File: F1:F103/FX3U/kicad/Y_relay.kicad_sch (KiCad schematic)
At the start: 3 parts, among them K2 HF46F

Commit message: End schematics
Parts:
- renumbered D25 to D30, K2 to K6, R3 to R75
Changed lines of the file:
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@@
 		(on_board yes)
 		(dnp no)
-		(property "Reference" "R3"
+		(property "Reference" "R75"
 			(at 64.135 46.99 90)
 			(effects
@@
 		(dnp no)
 		(fields_autoplaced yes)
-		(property "Reference" "K2"
+		(property "Reference" "K6"
 			(at 99.187 48.3178 0)
 			(effects
@@
 				(path "/b583aae5-8eb0-4221-b485-3f768bd7f89b/1c43d7a4-ec7a-47bb-8132-9a3f4ab13e61"
 					(reference "K9")
+					(unit 1)
+				)
+				(path "/b583aae5-8eb0-4221-b485-3f768bd7f89b/448100fa-8d41-4af2-bc0f-6a1f6a77b73d"
+					(reference "K1")
 					(unit 1)
 				)
@@
 		(on_board yes)
 		(dnp no)
-		(property "Reference" "D25"
+		(property "Reference" "D30"
 			(at 71.755 52.07 0)
 			(effects

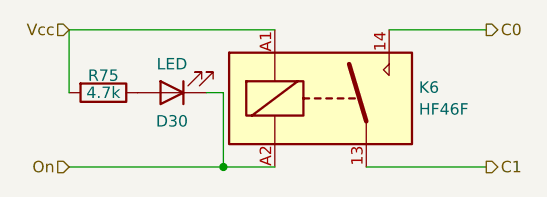
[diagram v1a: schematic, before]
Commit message: new kicad format
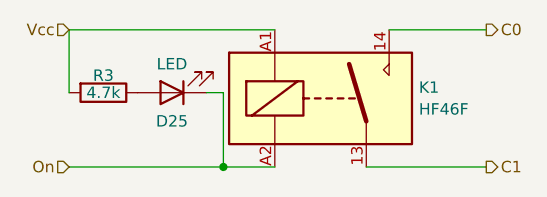
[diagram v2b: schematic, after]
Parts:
- renumbered D30 to D25, K6 to K1, R75 to R3
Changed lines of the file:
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@@
 (kicad_sch
-	(version 20231120)
+	(version 20250114)
 	(generator "eeschema")
-	(generator_version "8.0")
+	(generator_version "9.0")
 	(paper "A4")
 	(junction
@@
 		(shape input)
 		(at 60.325 41.91 180)
-		(fields_autoplaced yes)
 		(effects
 			(font
@@
 		(shape input)
 		(at 60.3276 57.15 180)
-		(fields_autoplaced yes)
 		(effects
 			(font
@@
 		(shape output)
 		(at 106.68 41.91 0)
-		(fields_autoplaced yes)
 		(effects
 			(font
@@
 		(shape output)
 		(at 106.68 57.15 0)
-		(fields_autoplaced yes)
 		(effects
 			(font
@@
 		(on_board yes)
 		(dnp no)
-		(property "Reference" "R75"
+		(property "Reference" "R3"
 			(at 64.135 46.99 90)
 			(effects
@@
 		(dnp no)
 		(fields_autoplaced yes)
-		(property "Reference" "K6"
+		(property "Reference" "K1"
 			(at 99.187 48.3178 0)
 			(effects
@@
 		(on_board yes)
 		(dnp no)
-		(property "Reference" "D30"
+		(property "Reference" "D25"
 			(at 71.755 52.07 0)
 			(effects
